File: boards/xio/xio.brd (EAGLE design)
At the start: 170 x 170 mm, 91 parts, among them U1 24 MHz Osc. (F535L-24), X1 PCI-E-164SOCKET, X2 PCI-E-164SOCKET, X3 PCI-E-164SOCKET, X4 PCI-E-164SOCKET, X5 PCI-E-164SOCKET, X6 PCI-E-164SOCKET, X7 PCI-E-164SOCKET

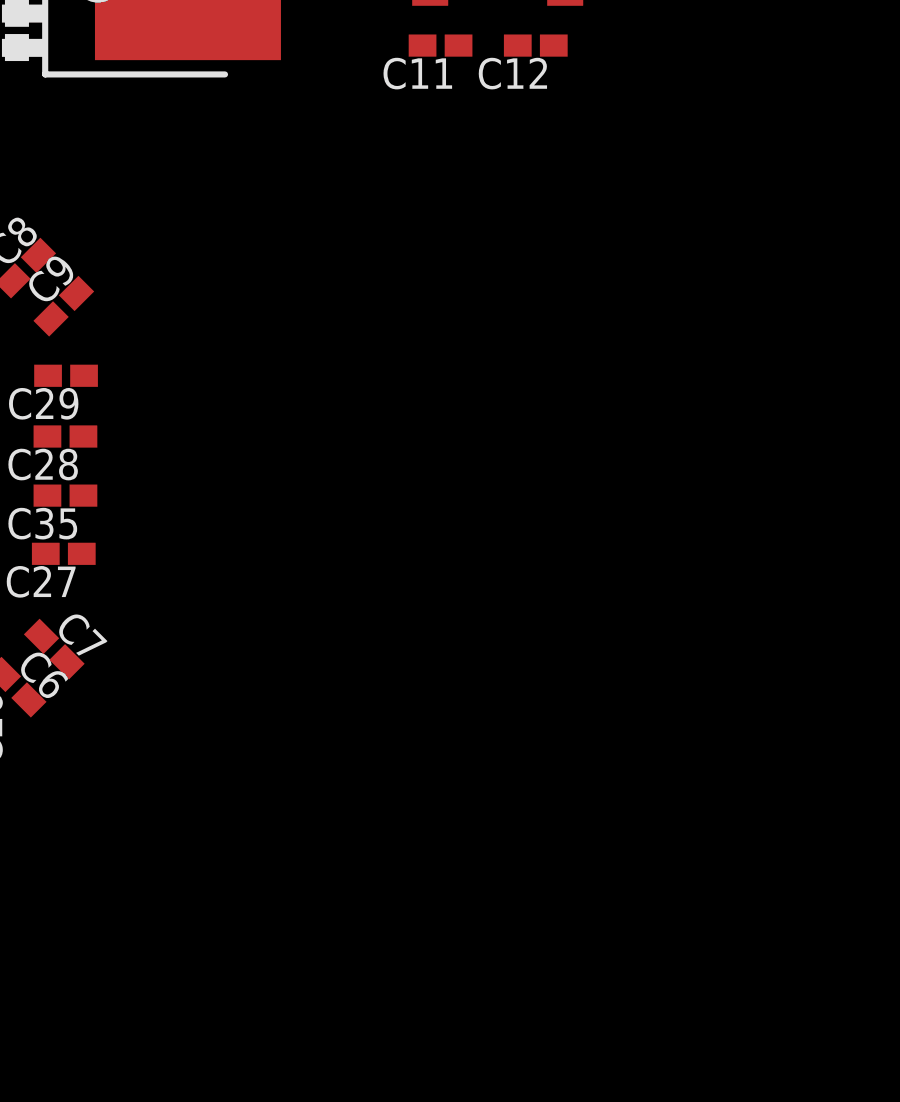
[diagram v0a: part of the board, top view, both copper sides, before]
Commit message: Start on the XMOS SDRAM
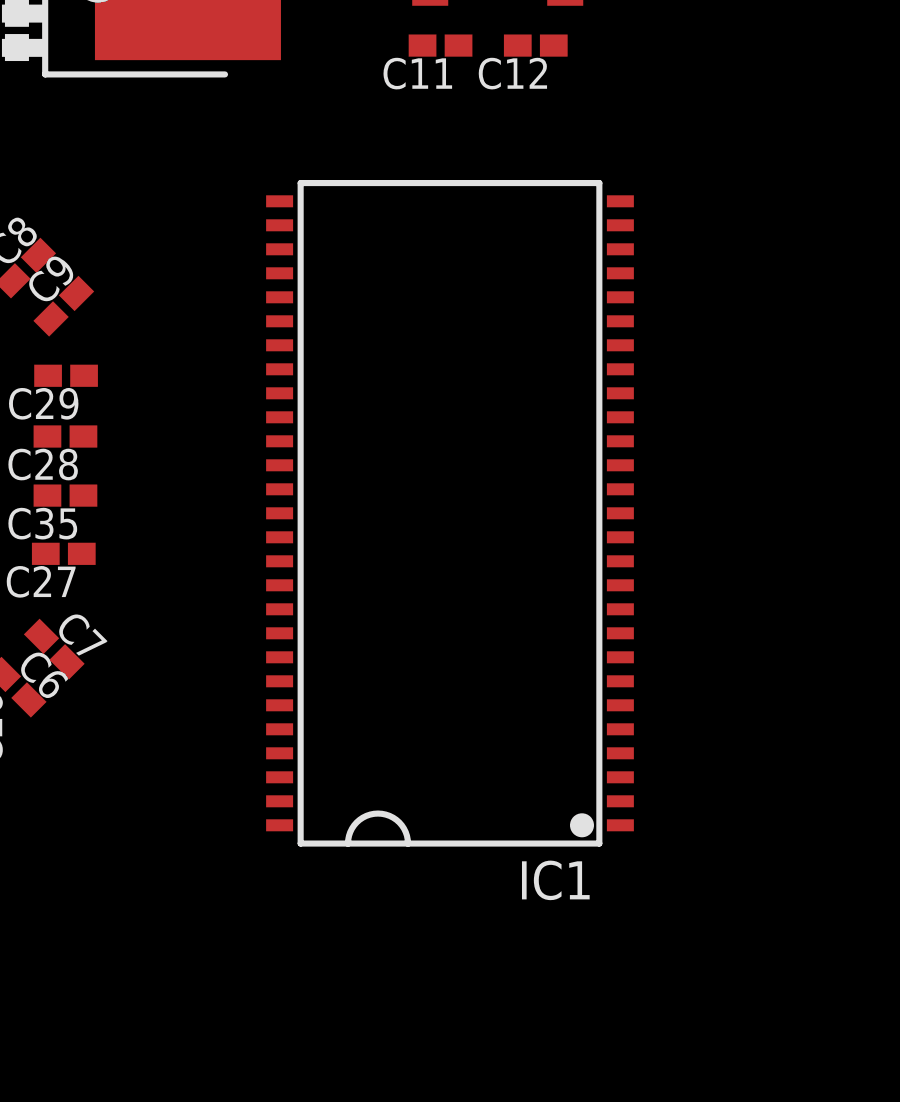
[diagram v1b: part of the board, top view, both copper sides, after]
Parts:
- added IC1: AS4C16M16SA-C, memory-micron:TSOP54-400
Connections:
- new net VDDQ: IC1.3, IC1.43, IC1.49, IC1.9
- new net VSS: IC1.28, IC1.41, IC1.54
- new net VSSQ: IC1.12, IC1.46, IC1.52, IC1.6
- net VDD: now also IC1.1, IC1.14, IC1.27
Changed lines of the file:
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@@
 <attribute name="SPICEPREFIX" value="R" x="156.845" y="105.41" size="1.778" layer="27" rot="R270" display="off"/>
+</element>
+<element name="IC1" library="memory-micron" library_urn="urn:adsk.eagle:library:274" package="TSOP54-400" package3d_urn="urn:adsk.eagle:package:18739/1" value="AS4C16M16SA-C" x="48.3997" y="137.7442" rot="R90">
+<attribute name="MF" value="" x="48.3997" y="137.7442" size="1.778" layer="27" rot="R90" display="off"/>
+<attribute name="MPN" value="" x="48.3997" y="137.7442" size="1.778" layer="27" rot="R90" display="off"/>
+<attribute name="OC_FARNELL" value="unknown" x="48.3997" y="137.7442" size="1.778" layer="27" rot="R90" display="off"/>
+<attribute name="OC_NEWARK" value="unknown" x="48.3997" y="137.7442" size="1.778" layer="27" rot="R90" display="off"/>
 </element>
 </elements>
@@
 <contactref element="C14" pad="1"/>
 <contactref element="U$6" pad="5"/>
+<contactref element="IC1" pad="1"/>
+<contactref element="IC1" pad="14"/>
+<contactref element="IC1" pad="27"/>
 <wire x1="32.365" y1="154.41" x2="31.415" y2="155.55" width="0" layer="19" extent="1-1"/>
 <wire x1="32.351221875" y1="146.6358" x2="32.365" y2="154.41" width="0" layer="19" extent="1-1"/>
@@
 <wire x1="36.126221875" y1="136.3933" x2="36.181221875" y2="138.3333" width="0" layer="19" extent="1-1"/>
 <wire x1="13.97" y1="159.265" x2="24.413721875" y2="146.6358" width="0" layer="19" extent="1-1"/>
+<wire x1="54.0797" y1="148.1442" x2="27.588721875" y2="131.9133" width="0" layer="19" extent="1-1"/>
+<wire x1="54.0797" y1="137.7442" x2="54.0797" y2="148.1442" width="0" layer="19" extent="1-1"/>
+<wire x1="54.0797" y1="127.3442" x2="54.0797" y2="137.7442" width="0" layer="19" extent="1-1"/>
 </signal>
 <signal name="+3V3">
@@
 <wire x1="164.465" y1="109.22" x2="164.465" y2="105.91" width="0" layer="19" extent="1-1"/>
 </signal>
+<signal name="VDDQ">
+<contactref element="IC1" pad="3"/>
+<contactref element="IC1" pad="9"/>
+<contactref element="IC1" pad="43"/>
+<contactref element="IC1" pad="49"/>
+<wire x1="54.0797" y1="133.7442" x2="54.0797" y2="128.9442" width="0" layer="19" extent="1-1"/>
+<wire x1="42.7197" y1="131.3442" x2="54.0797" y2="128.9442" width="0" layer="19" extent="1-1"/>
+<wire x1="42.7197" y1="136.1442" x2="42.7197" y2="131.3442" width="0" layer="19" extent="1-1"/>
+</signal>
+<signal name="VSSQ">
+<contactref element="IC1" pad="6"/>
+<contactref element="IC1" pad="12"/>
+<contactref element="IC1" pad="46"/>
+<contactref element="IC1" pad="52"/>
+<wire x1="54.0797" y1="136.1442" x2="54.0797" y2="131.3442" width="0" layer="19" extent="1-1"/>
+<wire x1="42.7197" y1="128.9442" x2="54.0797" y2="131.3442" width="0" layer="19" extent="1-1"/>
+<wire x1="42.7197" y1="133.7442" x2="42.7197" y2="128.9442" width="0" layer="19" extent="1-1"/>
+</signal>
+<signal name="VSS">
+<contactref element="IC1" pad="28"/>
+<contactref element="IC1" pad="41"/>
+<contactref element="IC1" pad="54"/>
+<wire x1="42.7197" y1="137.7442" x2="42.7197" y2="127.3442" width="0" layer="19" extent="1-1"/>
+<wire x1="42.7197" y1="148.1442" x2="42.7197" y2="137.7442" width="0" layer="19" extent="1-1"/>
+</signal>
 </signals>

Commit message: Checkpoint
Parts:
- added DBG0, DBG1: ok33, led:CHIP-LED0805
- added IC2: 74LVC1G02DBV, 74xx-little-de:SOT23-5
- added MEM_ID: 209-2MS, special:EDG-02
- added PID: 209-3MS, special:EDG-03
- added R10, R11: 10K, rcl:R0402
- added R12, R13: 33R, rcl:R0402
- added R14, R15, R16, R17, R18: 47k, rcl:R0402
- added R20, R21: 1K, rcl:R0402
- moved XTAG1 168.2 mm to (168.9, 140.8), turned to 270 degrees
- moved JTAG5V1 162.7 mm to (164.2, 157.4), turned to 180 degrees
- moved R5 148.3 mm to (157.4, 133.9), turned to 270 degrees
- moved R4 147.9 mm to (158.0, 141.2), turned to 180 degrees
- moved U$5 147.6 mm to (158.0, 143.4), turned to 90 degrees
- moved C16 147.5 mm to (158.0, 145.6), turned to 0 degrees
- moved C33 144.0 mm to (154.5, 130.4), turned to 180 degrees
- moved U$6 142.6 mm to (154.5, 133.9), turned to 180 degrees
- moved C36 141.1 mm to (154.2, 136.7), turned to 0 degrees
- moved C17 137.0 mm to (151.7, 133.9), turned to 270 degrees
- moved RESET_SW 130.5 mm to (146.9, 127.9), turned to 180 degrees
- moved C4 129.4 mm to (147.7, 158.9), turned to 45 degrees
- moved C23 128.9 mm to (147.9, 155.9), turned to 0 degrees
- moved C34 128.5 mm to (148.0, 153.8), turned to 0 degrees
- moved C22 128.0 mm to (147.9, 152.1), turned to 0 degrees
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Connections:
- removed net 3V3: C10.1, C2.1, C3.1, C34.1, C4.1, C5.1, C6.1, C7.1, C8.1, C9.1
- removed net VDDQ: IC1.3, IC1.43, IC1.49, IC1.9
- removed net VSS: IC1.28, IC1.41, IC1.54
- removed net VSSQ: IC1.12, IC1.46, IC1.52, IC1.6
- new net MEM0: MEM_ID.1, R18.1, U$1.L2
- new net MEM1: MEM_ID.2, R17.1, U$1.L1
- new net N$11: IC1.37, R11.1
- new net N$12: R12.1, U$1.M3
- new net N$13: IC1.19, R10.2
- new net N$14: R13.1, U$1.N2
- new net N$15: DBG0.A, U$1.W8
- new net N$16: DBG0.C, R21.2
- new net N$18: DBG1.A, U$1.U7
- new net N$19: DBG1.C, R20.2
- new net N$8: IC1.15, IC1.39, IC2.4
- new net PID0: PID.1, R16.1, U$1.N3
- new net PID1: PID.2, R15.1, U$1.P2
- new net PID2: PID.3, R14.1, U$1.P1
- new net VCC: IC2.5
- new net XMOS_ADQ0: IC1.2, IC1.23, U$1.T17
- new net XMOS_ADQ1: IC1.24, IC1.4, U$1.R17
- new net XMOS_ADQ10: IC1.22, IC1.45, U$1.T2
- new net XMOS_ADQ11: IC1.35, IC1.47, U$1.R3
- new net XMOS_ADQ12: IC1.36, IC1.48, U$1.T3
- new net XMOS_ADQ13: IC1.20, IC1.50, U$1.U3
- new net XMOS_ADQ14: IC1.21, IC1.51, U$1.W11
- new net XMOS_ADQ15: IC1.53, U$1.V11
- new net XMOS_ADQ2: IC1.25, IC1.5, U$1.T18
- new net XMOS_ADQ3: IC1.26, IC1.7, U$1.R18
- new net XMOS_ADQ4: IC1.29, IC1.8, U$1.R19
- new net XMOS_ADQ5: IC1.10, IC1.30, U$1.P17
- new net XMOS_ADQ6: IC1.11, IC1.31, U$1.F17
- new net XMOS_ADQ7: IC1.13, IC1.32, U$1.F18
- new net XMOS_ADQ8: IC1.33, IC1.42, U$1.V12
- new net XMOS_ADQ9: IC1.34, IC1.44, U$1.W12
- new net XMOS_CAS: IC1.17, IC2.1, U$1.F19
- new net XMOS_CLK: IC1.38, U$1.C8
- new net XMOS_RAS: IC1.18, U$1.E19
- new net XMOS_WE: IC1.16, IC2.2, U$1.C7
- net +3V3: now also C10.1, C2.1, C3.1, C34.1, C4.1, C5.1, C6.1, C7.1, C8.1, C9.1, IC1.1, IC1.14, IC1.27, IC1.3, IC1.43, IC1.49, IC1.9, MEM_ID.3, MEM_ID.4, PID.4, PID.5, PID.6, R11.2
- net GND: now also IC1.12, IC1.28, IC1.41, IC1.46, IC1.52, IC1.54, IC1.6, IC2.3, R10.1, R14.2, R15.2, R16.2, R17.2, R18.2, R20.1, R21.1
- net JTAG_DN0: now also U$1.M2
- net JTAG_DN1: now also U$1.M1
- net JTAG_UP0: now also R12.2
- net JTAG_UP1: now also R13.2
- net UART_RX: now also U$1.W3
- net UART_TX: now also U$1.V1
- net VDD: no longer IC1.1, IC1.14, IC1.27
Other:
- board text added: "- Overlap pads - SIO connector - STM32F7 etc - STM32F7 SDRAM"
- board text removed: "- Overlap pads - PBI id - memory type id - SIO connector - STM32F7 etc - 2x SDRAM (match XMOS library)"

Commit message: Start to add VHDCI interfaces (drivers to PIO board and voltage conversion to 3.3v)
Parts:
- added C51, C52, C53, C54, C55, C56: 0.1uF, rcl:C0402
- added D2: (no value), SparkFun-DiscreteSemi:DIODE-1N4001-KIT
- added IC3, IC4, IC5, IC6, IC7: IDTQS3245QSOP20, IDTQS_3245QG:QSOP20
- added U$15: CY74FCT827TSSOP24, sjg-logic:SSOP24
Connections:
- removed net VHDCI_NC1: U$14.P1, X1.A67, X2.A67, X3.A67, X4.A67, X5.A67, X6.A67, X7.A67
- removed net VHDCI_NC2: U$14.P2, X1.A68, X2.A68, X3.A68, X4.A68, X5.A68, X6.A68, X7.A68
- removed net VHDCI_NC3: U$14.P3, X1.A69, X2.A69, X3.A69, X4.A69, X5.A69, X6.A69, X7.A69
- removed net VHDCI_NC4: U$14.P4, X1.A70, X2.A70, X3.A70, X4.A70, X5.A70, X6.A70, X7.A70
- removed net VHDCI_NC5: U$14.P5, X1.A71, X2.A71, X3.A71, X4.A71, X5.A71, X6.A71, X7.A71
- removed net VHDCI_NC6: U$14.P6, X1.A72, X2.A72, X3.A72, X4.A72, X5.A72, X6.A72, X7.A72
- removed net VHDCI_NC7: U$14.P7, X1.A73, X2.A73, X3.A73, X4.A73, X5.A73, X6.A73, X7.A73
- new net +4.3V: C52.1, C53.1, C54.1, C55.1, C56.1, D2.C, IC3.20, IC4.20, IC5.20, IC6.20, IC7.20
- new net DRV_EXSEL: U$14.P27, U$15.17
- new net DRV_IRQ: U$14.P28, U$15.16
- new net DRV_MPD: U$14.P26, U$15.18
- new net DRV_OUT0: U$14.P5, U$15.23
- new net DRV_OUT1: U$14.P6, U$15.22
- new net DRV_OUT2: U$14.P7, U$15.21
- new net DRV_RD4: U$14.P25, U$15.19
- new net DRV_RD5: U$14.P24, U$15.20
- new net VHDCI_IN0: U$14.P1, X1.A50, X2.A50, X3.A50, X4.A50, X5.A50, X6.A50, X7.A50
- new net VHDCI_IN1: U$14.P2, X1.A51, X2.A51, X3.A51, X4.A51, X5.A51, X6.A51, X7.A51
- new net VHDCI_IN2: U$14.P3, X1.A52, X2.A52, X3.A52, X4.A52, X5.A52, X6.A52, X7.A52
- new net VHDCI_IN3: U$14.P4, X1.A53, X2.A53, X3.A53, X4.A53, X5.A53, X6.A53, X7.A53
- new net VHDCI_OUT0: U$15.2, X1.A71, X2.A71, X3.A71, X4.A71, X5.A71, X6.A71, X7.A71
- new net VHDCI_OUT1: U$15.3, X1.A72, X2.A72, X3.A72, X4.A72, X5.A72, X6.A72, X7.A72
- new net VHDCI_OUT2: U$15.4, X1.A73, X2.A73, X3.A73, X4.A73, X5.A73, X6.A73, X7.A73
- net +5V: now also C51.1, D2.A, U$15.10, U$15.11, U$15.24
- net GND: now also C51.2, C52.2, C53.2, C54.2, C55.2, C56.2, IC3.10, IC3.19, IC4.10, IC4.19, IC5.10, IC5.19, IC6.10, IC6.19, IC7.10, IC7.19, U$15.1, U$15.12, U$15.13
- net VHDCI_EXSEL: now also U$15.8; no longer U$14.P27
- net VHDCI_IRQ: now also U$15.9, X1.A54, X2.A54, X3.A54, X4.A54, X5.A54, X6.A54, X7.A54; no longer U$14.P28, X1.A50, X2.A50, X3.A50, X4.A50, X5.A50, X6.A50, X7.A50
- net VHDCI_J1_1: now also X1.A55, X2.A55, X3.A55, X4.A55, X5.A55, X6.A55, X7.A55; no longer X1.A51, X2.A51, X3.A51, X4.A51, X5.A51, X6.A51, X7.A51
- net VHDCI_J1_2: now also X1.A56, X2.A56, X3.A56, X4.A56, X5.A56, X6.A56, X7.A56; no longer X1.A52, X2.A52, X3.A52, X4.A52, X5.A52, X6.A52, X7.A52
- net VHDCI_J1_3: now also X1.A57, X2.A57, X3.A57, X4.A57, X5.A57, X6.A57, X7.A57; no longer X1.A53, X2.A53, X3.A53, X4.A53, X5.A53, X6.A53, X7.A53
- net VHDCI_J1_4: now also X1.A58, X2.A58, X3.A58, X4.A58, X5.A58, X6.A58, X7.A58; no longer X1.A54, X2.A54, X3.A54, X4.A54, X5.A54, X6.A54, X7.A54
- net VHDCI_J1_5: now also X1.A59, X2.A59, X3.A59, X4.A59, X5.A59, X6.A59, X7.A59; no longer X1.A55, X2.A55, X3.A55, X4.A55, X5.A55, X6.A55, X7.A55
- net VHDCI_J1_A1: now also X1.A60, X2.A60, X3.A60, X4.A60, X5.A60, X6.A60, X7.A60; no longer X1.A56, X2.A56, X3.A56, X4.A56, X5.A56, X6.A56, X7.A56
- net VHDCI_J1_A2: now also X1.A61, X2.A61, X3.A61, X4.A61, X5.A61, X6.A61, X7.A61; no longer X1.A57, X2.A57, X3.A57, X4.A57, X5.A57, X6.A57, X7.A57
- net VHDCI_J2_1: now also X1.A62, X2.A62, X3.A62, X4.A62, X5.A62, X6.A62, X7.A62; no longer X1.A58, X2.A58, X3.A58, X4.A58, X5.A58, X6.A58, X7.A58
- net VHDCI_J2_2: now also X1.A63, X2.A63, X3.A63, X4.A63, X5.A63, X6.A63, X7.A63; no longer X1.A59, X2.A59, X3.A59, X4.A59, X5.A59, X6.A59, X7.A59
- net VHDCI_J2_3: now also X1.A64, X2.A64, X3.A64, X4.A64, X5.A64, X6.A64, X7.A64; no longer X1.A60, X2.A60, X3.A60, X4.A60, X5.A60, X6.A60, X7.A60
- net VHDCI_J2_4: now also X1.A65, X2.A65, X3.A65, X4.A65, X5.A65, X6.A65, X7.A65; no longer X1.A61, X2.A61, X3.A61, X4.A61, X5.A61, X6.A61, X7.A61
- net VHDCI_J2_5: now also X1.A66, X2.A66, X3.A66, X4.A66, X5.A66, X6.A66, X7.A66; no longer X1.A62, X2.A62, X3.A62, X4.A62, X5.A62, X6.A62, X7.A62
- net VHDCI_J2_A1: now also X1.A67, X2.A67, X3.A67, X4.A67, X5.A67, X6.A67, X7.A67; no longer X1.A63, X2.A63, X3.A63, X4.A63, X5.A63, X6.A63, X7.A63
- net VHDCI_J2_A2: now also X1.A68, X2.A68, X3.A68, X4.A68, X5.A68, X6.A68, X7.A68; no longer X1.A64, X2.A64, X3.A64, X4.A64, X5.A64, X6.A64, X7.A64
- net VHDCI_MPD: now also U$15.7, X1.A69, X2.A69, X3.A69, X4.A69, X5.A69, X6.A69, X7.A69; no longer U$14.P26, X1.A65, X2.A65, X3.A65, X4.A65, X5.A65, X6.A65, X7.A65
- net VHDCI_MTR_CTRL: now also X1.A70, X2.A70, X3.A70, X4.A70, X5.A70, X6.A70, X7.A70; no longer X1.A66, X2.A66, X3.A66, X4.A66, X5.A66, X6.A66, X7.A66
- net VHDCI_RD4: now also U$15.6; no longer U$14.P25
- net VHDCI_RD5: now also U$15.5; no longer U$14.P24
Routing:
- removed copper zone on layer 2, net GND

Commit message: Add in the voltage-level translation between 5v and 3.3v for the XMOS VHDCI bus
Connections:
- new net 3V3_!EXSEL!: IC6.17, U$1.C1
- new net 3V3_!HALT!: IC7.18, U$1.E1
- new net 3V3_!IRQ!: IC6.16, U$1.C2
- new net 3V3_!MPD!: IC6.15, U$1.D2
- new net 3V3_!REF!: IC7.11, U$1.E2
- new net 3V3_!RST!: IC6.12, U$1.E3
- new net 3V3_A0: IC3.18, U$1.P19
- new net 3V3_A1: IC3.17, U$1.P18
- new net 3V3_A10: IC4.16, U$1.K18
- new net 3V3_A11: IC4.15, U$1.K17
- new net 3V3_A12: IC4.14, U$1.J17
- new net 3V3_A13: IC4.13, U$1.J18
- new net 3V3_A14: IC4.12, U$1.J19
- new net 3V3_A15: IC4.11, U$1.H19
- new net 3V3_A2: IC3.16, U$1.N17
- new net 3V3_A3: IC3.15, U$1.N18
- new net 3V3_A4: IC3.14, U$1.M17
- new net 3V3_A5: IC3.13, U$1.M18
- new net 3V3_A6: IC3.12, U$1.M19
- new net 3V3_A7: IC3.11, U$1.L19
- new net 3V3_A8: IC4.18, U$1.L18
- new net 3V3_A9: IC4.17, U$1.L17
- new net 3V3_CLK: IC6.18, U$1.B1
- new net 3V3_D0: IC5.18, U$1.C18
- new net 3V3_D1: IC5.17, U$1.C19
- new net 3V3_D2: IC5.16, U$1.C17
- new net 3V3_D3: IC5.15, U$1.A17
- new net 3V3_D4: IC5.14, U$1.C16
- new net 3V3_D5: IC5.13, U$1.C15
- new net 3V3_D6: IC5.12, U$1.B17
- new net 3V3_D7: IC5.11, U$1.B16
- new net 3V3_IN0: IC7.17, U$1.H18
- new net 3V3_IN1: IC7.16, U$1.H17
- new net 3V3_IN2: IC7.15, U$1.G17
- new net 3V3_OUT0: IC7.14, U$1.W6
- new net 3V3_OUT1: IC7.13, U$1.V6
- new net 3V3_OUT2: IC7.12, U$1.V7
- new net 3V3_R/!W!: IC6.11, U$1.D3
- new net 3V3_RD4: IC6.14, U$1.D17
- new net 3V3_RD5: IC6.13, U$1.D18
- net N$2: now also U$1.U2
- net VHDCI_A00: now also IC3.2
- net VHDCI_A01: now also IC3.3
- net VHDCI_A02: now also IC3.4
- net VHDCI_A03: now also IC3.5
- net VHDCI_A04: now also IC3.6
- net VHDCI_A05: now also IC3.7
- net VHDCI_A06: now also IC3.8
- net VHDCI_A07: now also IC3.9
- net VHDCI_A08: now also IC4.2
- net VHDCI_A09: now also IC4.3
- net VHDCI_A10: now also IC4.4
- net VHDCI_A11: now also IC4.5
- net VHDCI_A12: now also IC4.6
- net VHDCI_A13: now also IC4.7
- net VHDCI_A14: now also IC4.8
- net VHDCI_A15: now also IC4.9
- net VHDCI_CLK: now also IC6.2
- net VHDCI_D00: now also IC5.2
- net VHDCI_D01: now also IC5.3
- net VHDCI_D02: now also IC5.4
- net VHDCI_D03: now also IC5.5
- net VHDCI_D04: now also IC5.6
- net VHDCI_D05: now also IC5.7
- net VHDCI_D06: now also IC5.8
- net VHDCI_D07: now also IC5.9
- net VHDCI_EXSEL: now also IC6.3
- net VHDCI_HALT: now also IC7.2
- net VHDCI_IN0: now also IC7.3
- net VHDCI_IN1: now also IC7.4
- net VHDCI_IN2: now also IC7.5
- net VHDCI_IRQ: now also IC6.4
- net VHDCI_MPD: now also IC6.5
- net VHDCI_OUT0: now also IC7.6
- net VHDCI_OUT1: now also IC7.7
- net VHDCI_OUT2: now also IC7.8
- net VHDCI_RD4: now also IC6.6
- net VHDCI_RD5: now also IC6.7
- net VHDCI_REF: now also IC7.9
- net VHDCI_RST: now also IC6.8
- net VHDCI_RW: now also IC6.9

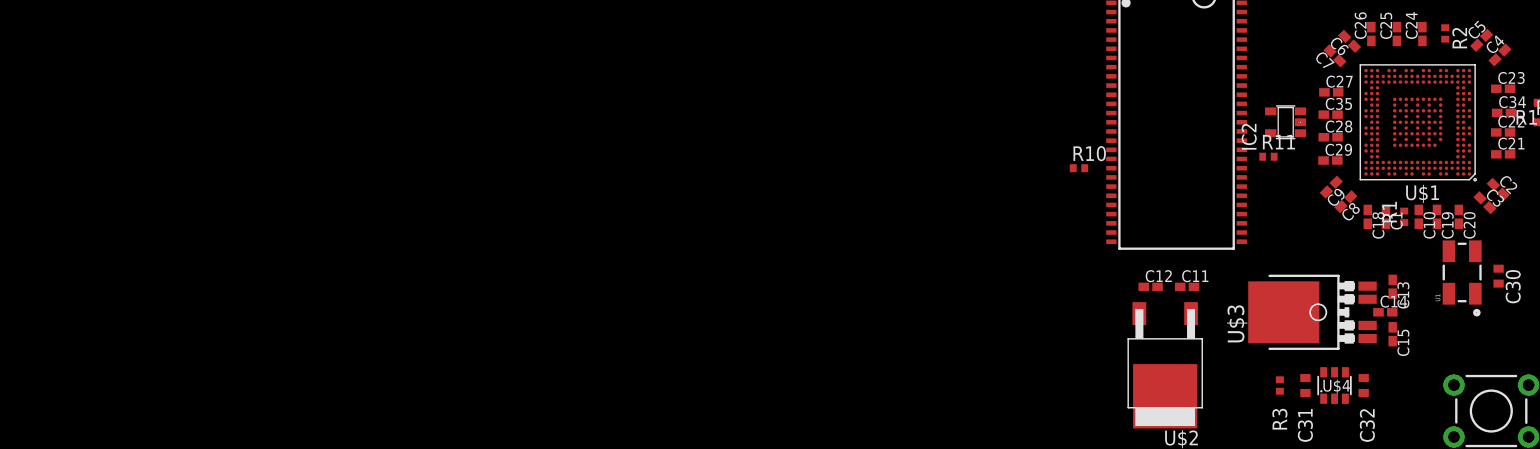
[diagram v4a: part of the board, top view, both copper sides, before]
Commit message: Add in the STM32 components
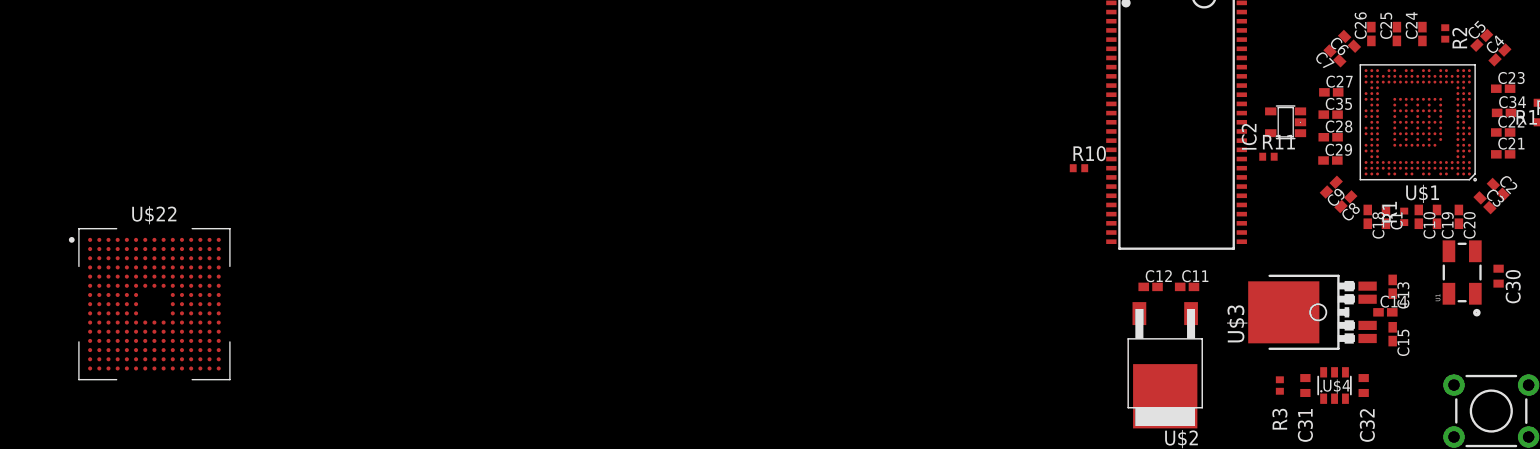
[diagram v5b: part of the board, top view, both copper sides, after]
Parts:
- added U$22: STM32F777N, sjg-stm32:BGA216C80P15X15_1300X1300X110
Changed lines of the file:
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@@
 <element name="IC7" library="IDTQS_3245QG" package="QSOP20" value="IDTQS3245QSOP20" x="144.145" y="109.855"/>
 <element name="C56" library="rcl" package="C0402" value="0.1uF" x="139.7" y="114.3" rot="R180"/>
+<element name="U$22" library="sjg-stm32" package="BGA216C80P15X15_1300X1300X110" package3d_urn="urn:adsk.eagle:package:3202291/1" value="STM32F777N" x="30.48" y="137.16"/>
 </elements>
 <signals>
